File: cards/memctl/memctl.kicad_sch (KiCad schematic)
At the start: 108 parts, among them J1 BUS, J2 LINK, Q1 2N7000, Q10 2N7000, Q11 2N7000, Q12 2N7000, Q13 2N7000, Q14 2N7000, Q15 2N7000, Q16 2N7000, Q17 2N7000, Q18 2N7000, Q19 2N7000, Q2 2N7000, Q20 2N7000, Q21 2N7000, Q22 2N7000, Q23 2N7000, Q24 2N7000, Q25 2N7000, Q26 2N7000, Q27 2N7000, Q28 2N7000, Q29 2N7000, Q3 2N7000, Q30 2N7000, Q31 2N7000, Q32 2N7000, Q33 2N7000, Q34 2N7000, Q35 2N7000, Q36 2N7000, Q37 2N7000, Q38 2N7000, Q39 2N7000, Q4 2N7000, Q40 2N7000, Q41 2N7000, Q42 2N7000, Q43 2N7000, Q44 2N7000, Q45 2N7000, Q46 2N7000, Q47 2N7000, Q48 2N7000, Q49 2N7000, Q5 2N7000, Q50 2N7000, Q51 2N7000, Q52 2N7000, Q53 2N7000, Q54 2N7000, Q55 2N7000, Q56 2N7000, Q57 2N7000, Q58 2N7000, Q59 2N7000, Q6 2N7000, Q7 2N7000, Q8 2N7000, Q9 2N7000

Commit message: Memory control: the address latch and the write take a mid-tick pulse (D054)
gcd, list and logic at mixed-threshold seed 2, with the clock card in the
deck, each wrote its first STORE to the wrong slot (12, 9 and 15 instead
of 0) and computed faithfully from there. A probed rerun of gcd to 134 ms
(memctl PH1, ENM, MAR, slot 0's SEL, WRE and cells): at the rising edge
ending the MAI tick the sequencer stepped when CLK passed 2 V and AO put
the STORE data on the bus 10 us later; the memory control card's PH1 NOR
saw the edge only at 3 V, and its address-latch enable (MAI AND PH1)
closed 12 us after the bus had changed, so MAR took the data as the
address. The write window (MI AND PH1) had the same exposure. D037's rule,
"PH1 closes before the rising edge on which everything else changes",
holds only if every card sees the edge at the same instant; with a 35 us
edge and 0.8 to 3.0 V thresholds they did not (D053 sharpens the edge;
this commit takes the memory out of the race altogether).

memory.py, build_ctl (and the reference board in build): CLKD is CLK
through 100k into 2.2 nF, drawn on the sheet; MPH = NOR(CLK, NOT CLKD) is
high from the falling edge of CLK until CLKD decays past a threshold,
60 to 350 us. ENM = MAI AND MPH, MIN = NAND(MI, MPH). The latch closes and
the write ends hundreds of microseconds before the next rising edge, when
the bus and the control lines have been stable for 700 us. PH1/PH2 leave
the card (57 transistors, was 59). cards/memctl regenerated and re-routed:
DRC 0, 0 unconnected, renders read; the slot card is unchanged.

tb_memory: --race is the edge as the memory card saw it in the machine:
CLK rises over 35 us, the bus switches 10 us into the rise, the control
lines 100 us after it (they lag every edge by 60 to 170 us in the machine;
a first version switched them with the bus and MAI closed the latch
itself, no failure). The bench's clock now runs a cycle before the first
case so the first tick has its falling edge too. The gate-list n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
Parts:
- removed Q58, Q59: 2N7000, Package_TO_SOT_THT:TO-92_Inline_Wide, symbol Transistor_FET:2N7000
- added C3: 2.2n, Capacitor_THT:C_Disc_D5.0mm_W2.5mm_P2.50mm, symbol Device:C
- R12, R17, R22, R27, R29: value 47k -> 22k
- R13, R18, R23, R28: value 22k -> 47k
- R3: value 10k -> 47k
- R33: value 22k -> 4.7k
- R34: value 4.7k -> 22k
- R35: value 22k -> 1k
- R39: value 1k -> 100k
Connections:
- net +5V: now also R34.1; no longer R34.2, R39.1
- net BUS0#: now also Q4.2 (G); no longer Q6.2 (G)
- net BUS1#: now also Q5.2 (G); no longer Q7.2 (G)
- net BUS2#: now also Q6.2 (G); no longer Q8.2 (G)
- net BUS3#: now also Q7.2 (G); no longer Q9.2 (G)
- net CLK: now also R39.1; no longer Q1.2 (G)
- net D0: now also Q11.2 (G), Q12.2 (G), Q4.3 (D), R3.1; no longer Q13.2 (G), Q14.2 (G), Q6.3 (D), R4.1
- net D1: now also Q20.2 (G), Q21.2 (G), Q5.3 (D), R4.1; no longer Q22.2 (G), Q23.2 (G), Q7.3 (D), R5.1
- net D2: now also Q29.2 (G), Q30.2 (G), Q6.3 (D), R5.1; no longer Q31.2 (G), Q32.2 (G), Q8.3 (D), R6.1
- net D3: now also Q38.2 (G), Q39.2 (G), Q7.3 (D), R6.1; no longer Q40.2 (G), Q41.2 (G), Q9.3 (D), R7.1
- net ENM: now also Q10.3 (D), Q13.2 (G), Q14.2 (G), Q22.2 (G), Q23.2 (G), Q31.2 (G), Q32.2 (G), Q40.2 (G), Q41.2 (G), R8.2; no longer Q12.3 (D), Q15.2 (G), Q16.2 (G), Q24.2 (G), Q25.2 (G), Q33.2 (G), Q34.2 (G), Q42.2 (G), Q43.2 (G), R9.2
- net ENMN: now also Q10.2 (G), Q8.3 (D), R7.1; no longer Q10.3 (D), Q12.2 (G), R8.2
- net GND: now also Q10.1 (S), Q20.1 (S), Q29.1 (S), Q38.1 (S), Q47.1 (S), Q53.1 (S), C3.2; no longer Q12.1 (S), Q21.1 (S), Q30.1 (S), Q39.1 (S), Q51.1 (S), Q8.1 (S)
- net MAI: now also Q8.2 (G); no longer Q10.2 (G)
- net MAR0: now also Q16.3 (D), Q18.2 (G), Q47.2 (G), Q57.2 (G), R12.2; no longer Q18.3 (D), Q20.2 (G), Q49.2 (G), R13.1
- net MAR0N: now also Q47.3 (D), R29.2; no longer Q49.3 (D), R30.2
- net MAR0_dn: now also Q11.3 (D), Q15.2 (G), R9.2; no longer Q13.3 (D), Q17.2 (G), R10.2
- net MAR0_m1: now also Q12.3 (D), Q16.2 (G), R10.2; no longer Q14.3 (D), Q18.2 (G), R11.2
- net MAR0_m2: now also Q14.3 (D), Q19.2 (G), R11.2; no longer Q16.3 (D), Q21.2 (G), R12.2
- net MAR0_qn: now also Q17.2 (G), Q18.3 (D), R13.1; no longer Q19.2 (G), Q20.3 (D), R14.1
- net MAR1: now also Q25.3 (D), Q27.2 (G), Q48.2 (G), Q56.2 (G), R17.1; no longer Q27.3 (D), Q29.2 (G), Q50.2 (G), R18.2
- net MAR1N: now also Q48.3 (D), R30.2; no longer Q50.3 (D), R31.2
- net MAR1_dn: now also Q20.3 (D), Q24.2 (G), R14.1; no longer Q22.3 (D), Q26.2 (G), R15.1
- net MAR1_m1: now also Q21.3 (D), Q25.2 (G), R15.1; no longer Q23.3 (D), Q27.2 (G), R16.1
- net MAR1_m2: now also Q23.3 (D), Q28.2 (G), R16.1; no longer Q25.3 (D), Q30.2 (G), R17.1
- net MAR1_qn: now also Q26.2 (G), Q27.3 (D), R18.2; no longer Q28.2 (G), Q29.3 (D), R19.2
- net MAR2: now also Q34.3 (D), Q36.2 (G), Q49.2 (G), Q55.2 (G), R22.2; no longer Q36.3 (D), Q38.2 (G), Q51.2 (G), Q57.2 (G), R23.1
- net MAR2N: now also Q49.3 (D), R31.2; no longer Q51.3 (D), R32.2
- net MAR2_dn: now also Q29.3 (D), Q33.2 (G), R19.2; no longer Q31.3 (D), Q35.2 (G), R20.2
- net MAR2_m1: now also Q30.3 (D), Q34.2 (G), R20.2; no longer Q32.3 (D), Q36.2 (G), R21.2
- net MAR2_m2: now also Q32.3 (D), Q37.2 (G), R21.2; no longer Q34.3 (D), Q39.2 (G), R22.2
- net MAR2_qn: now also Q35.2 (G), Q36.3 (D), R23.1; no longer Q37.2 (G), Q38.3 (D), R24.1
- net MAR3: now also Q43.3 (D), Q45.2 (G), Q50.2 (G), Q54.2 (G), R27.1; no longer Q45.3 (D), Q47.2 (G), Q52.2 (G), Q56.2 (G), R28.2
- net MAR3N: now also Q50.3 (D), R32.2; no longer Q52.3 (D), R33.2
- net MAR3_dn: now also Q38.3 (D), Q42.2 (G), R24.1; no longer Q40.3 (D), Q44.2 (G), R25.1
- net MAR3_m1: now also Q39.3 (D), Q43.2 (G), R25.1; no longer Q41.3 (D), Q45.2 (G), R26.1
- net MAR3_m2: now also Q41.3 (D), Q46.2 (G), R26.1; no longer Q43.3 (D), Q48.2 (G), R27.1
- net MAR3_qn: now also Q44.2 (G), Q45.3 (D), R28.2; no longer Q46.2 (G), Q47.3 (D), R29.2
- net MI: now also Q51.2 (G); no longer Q53.2 (G)
- net MIN: now also Q51.3 (D), R33.2; no longer Q53.3 (D), R34.1
- net MO: now also Q53.2 (G); no longer Q55.2 (G)
- net MON: now also Q53.3 (D), R34.2; no longer Q55.3 (D), R35.1
- net at Q56.3 (D): now also D3.1 (K); no longer D1.1 (K)
- net at R38.1: now also D4.2 (A); no longer D3.2 (A)
- net at Q54.3 (D): now also D1.1 (K); no longer Q53.1 (S)
- net at Q57.3 (D): now also D4.1 (K); no longer D2.1 (K)
- net CLKD: now reaches R39.2
- net CLKD: now also Q1.2 (G), C3.1; no longer D4.2 (A)
- net at R37.1: now also D3.2 (A); no longer D2.2 (A)
- net at D1.2 (A): now also R35.1; no longer R36.1
- net CLKN renamed CLKDN
- net CLKDN: now also Q3.2 (G); no longer Q4.2 (G)
- net PH1 renamed MPH
- net MPH: now also Q52.2 (G), Q9.2 (G); no longer Q11.2 (G), Q5.2 (G), Q54.2 (G)
- removed net PH2: Q3.2 (G), Q4.3 (D), Q5.3 (D), R3.1
- new net: Q51.1 (S), Q52.3 (D)
- new net: Q30.1 (S), Q31.3 (D)
- new net: D2.1 (K), Q55.3 (D)
- new net: D2.2 (A), R36.1
- new net: Q12.1 (S), Q13.3 (D)
- new net: Q21.1 (S), Q22.3 (D)
- new net: Q39.1 (S), Q40.3 (D)
- new net: Q8.1 (S), Q9.3 (D)
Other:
- note added: "ADDRESS REGISTER: four transparent latches, open while MAI and MPH. MAR3..0 and their complements go to the slot cards over the ribbon; each card picks its address with jumpers."
- note added: "Cell: 2N7000 + 47k pull-up (NMOS, see docs/gate-cell.md). 57 transistors, 38 resistors, 4 LEDs, 100 x 100 mm (docs/cards.md). From the bus header: BUS3#..BUS0# (an address while MAI), MAI, MI, MO, CLK. To the slot cards over the LINK ribbon (2x6, chained along the eight slot cards): MAR3..0 and their complements, MIN (low = write allowed: MI and MPH), MON (low = read: MO). MAR is four transparent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"
- note added: "MID-TICK PULSE (D054): CLK through 100k into 2.2 nF gives CLKD, 0.22 ms behind CLK. MPH = NOR(CLK, NOT CLKD) is high from the falling edge of CLK until CLKD decays past a threshold (60 to 350 us): the address latch and the write windows"
- note added: "MID-TICK PULSE (D054): CLKD is CLK through 100k into 2.2 nF (drawn on the sheet); MPH = NOR(CLK, NOT CLKD) is high from the falling edge of CLK until CLKD decays past a threshold, 60 to 350 us: the address latch closes and the write ends in the middle of the tick, far from both edges"
- note added: "WRITE AND READ GATES for all slots: MIN low (write allowed) only while MI and MPH, so a write ends in the middle of the tick; MON low while MO. 4.7k on MIN: sixteen write lines on eight cards drop within microseconds of the pulse's end."
- note removed: "ADDRESS REGISTER: four transparent latches, open while MAI and PH1. MAR3..0 and their complements go to the slot cards over the ribbon; each card picks its address with jumpers."
- note removed: "Cell: 2N7000 + 47k pull-up (NMOS, see docs/gate-cell.md). 59 transistors, 39 resistors, 4 LEDs, 100 x 100 mm (docs/cards.md). From the bus header: BUS3#..BUS0# (an address while MAI), MAI, MI, MO, CLK. To the slot cards over the LINK ribbon (2x6, chained along the eight slot cards): MAR3..0 and their complements, MIN (low = write allowed: MI and PH1), MON (low = read: MO). MAR is four transparent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"
- note removed: "TWO-PHASE CLOCK: only PH1 is used here, to close the address latches and end the write before the rising edge"
- note removed: "WRITE AND READ GATES for all slots: MIN low (write allowed) only while MI and PH1, so a write ends at the clock edge; MON low while MO. 4.7k on MIN: sixteen write lines on eight cards drop within microseconds of the edge."

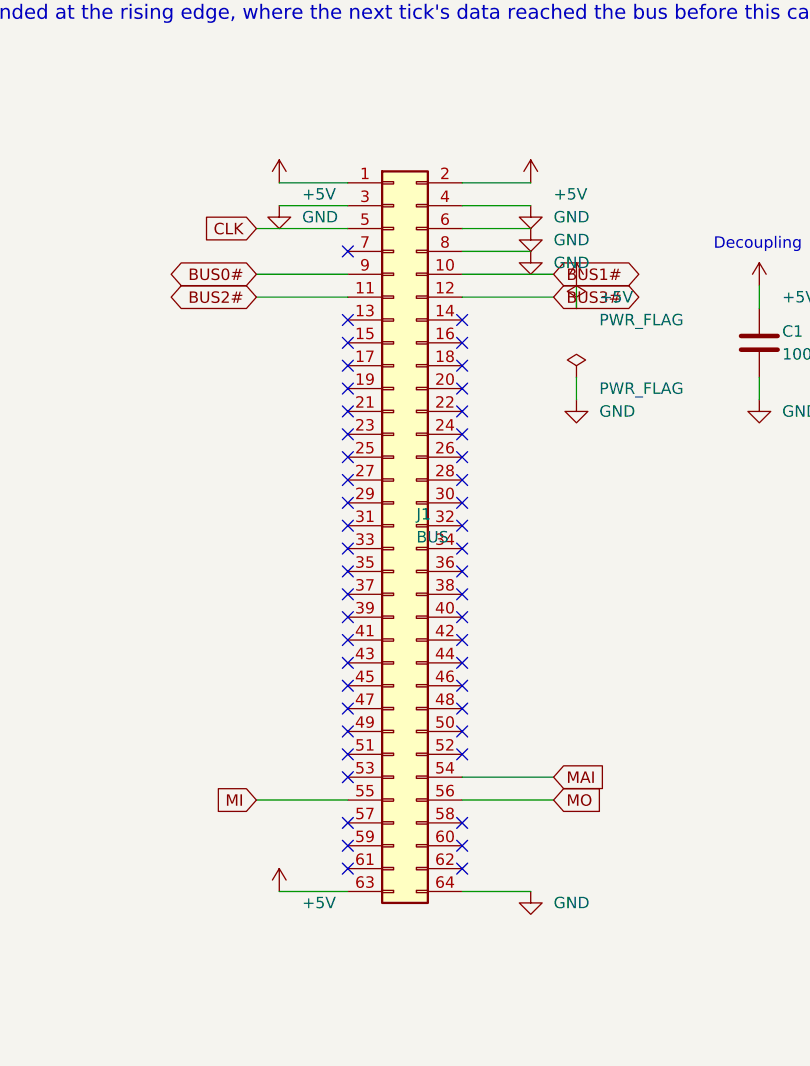
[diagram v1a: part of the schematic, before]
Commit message: The bus headers go on the back of all 26 boards, no track moved; the silkscreen refitted (D059, D062)
An IDC socket lies across its ribbon, so the ribbon could never run along a
row of cards as drawn. It runs behind them, and the 64-pin headers are
soldered on the back. This commit is that move, made in place on the routed
boards: no board was routed again.

How the header sits (D062): in the holes it had, turned over top to bottom,
notch toward the top edge. A pin of the odd row is then in the hole its even
neighbour had, so the two signals of every pair of pins change places: CLK
is pin 6, RST pin 8, +5V pins 1, 2 and 64. bus.py keeps both tables: PINS,
what the header's pins carry, and HOLES, what the copper was routed to.

The proof, on all 26 boards against 992a90f (sim/board_diff.py):
  netlist the same, element for element; every track, every via and every
  hole the same; each copper and mask layer differs by two pad shapes per
  header (pin 1's square went to the hole beside it, both on +5V) and the
  ground pour's outline round those two pads, nowhere else by more than a
  tenth of a micrometre.
sim/rebuild_check.py runs every builder into a scratch directory: each
writes the plan and the netlist that are committed, so a rebuild gives
this board. order_check.py --machine holds every pad of the 27 headers to
bus.py and requires them on the back.

What the move costs: on the ribbon RST had a ground conductor on both
sides; now one neighbour is BUS1#. tb_rst_neighbour.py puts the two lines
on the bench with every gate the routed boards hang on them: RST rises
0.28 to 0.43 V when BUS1# is released, against a lowest threshold of 0.8 V
(sim/results/rst_neighbour.md). The machine deck's crosstalk option now
couples the pins that are neighbours on the ribbon; the crosstalk stage of
the machine gate has to be run again on that order.

Silkscreen (pcb.fit_silk): every label to 1.0 mm where it has room, off
pads, vias, outlines and other labels, out from under the pa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
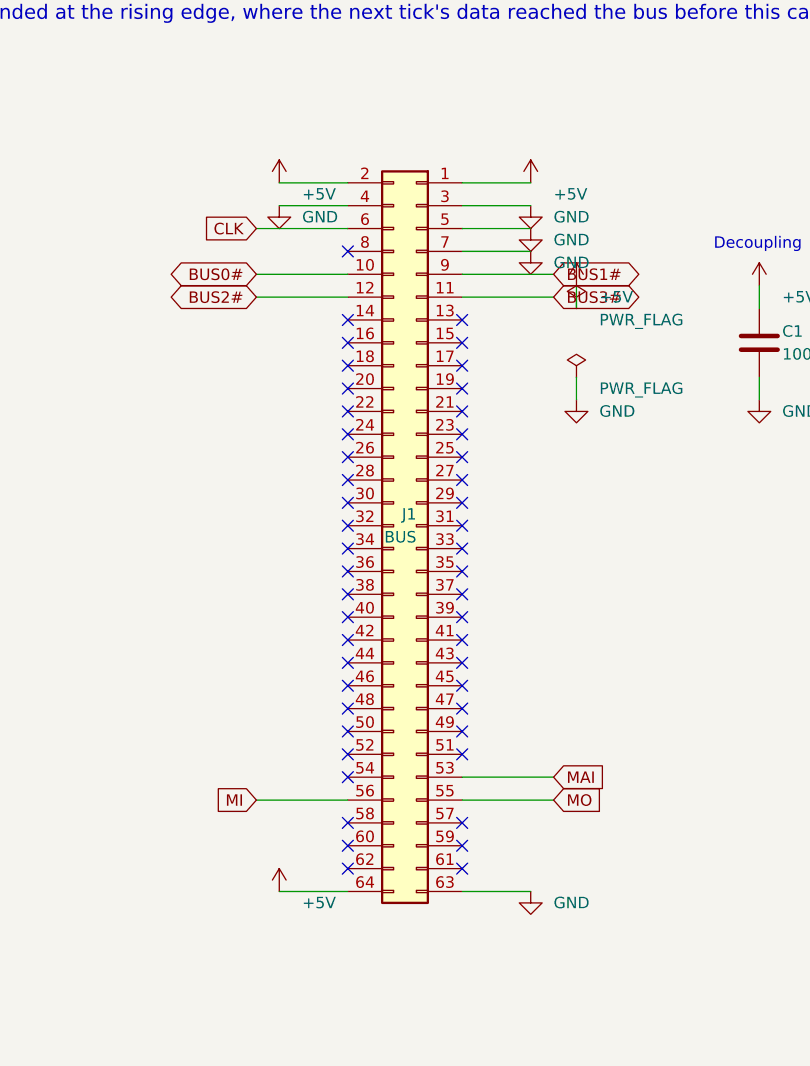
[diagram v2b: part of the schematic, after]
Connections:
- net +5V: now also J1.64 (Pin_64); no longer J1.63 (Pin_63)
- net BUS0#: now also J1.10 (Pin_10); no longer J1.9 (Pin_9)
- net BUS1#: now also J1.9 (Pin_9); no longer J1.10 (Pin_10)
- net BUS2#: now also J1.12 (Pin_12); no longer J1.11 (Pin_11)
- net BUS3#: now also J1.11 (Pin_11); no longer J1.12 (Pin_12)
- net CLK: now also J1.6 (Pin_6); no longer J1.5 (Pin_5)
- net GND: now also J1.5 (Pin_5), J1.63 (Pin_63), J1.7 (Pin_7); no longer J1.6 (Pin_6), J1.64 (Pin_64), J1.8 (Pin_8)
- net MAI: now also J1.53 (Pin_53); no longer J1.54 (Pin_54)
- net MI: now also J1.56 (Pin_56); no longer J1.55 (Pin_55)
- net MO: now also J1.55 (Pin_55); no longer J1.56 (Pin_56)
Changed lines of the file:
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@@
 	(symbol
 		(lib_id "Connector_Generic:Conn_02x32_Odd_Even")
-		(at 76.2 101.6 0)
+		(at 78.74 101.6 0)
+		(mirror y)
 		(unit 1)
 		(body_style 1)
